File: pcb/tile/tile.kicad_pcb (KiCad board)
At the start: 2 copper layers, 41.5 x 28 mm, 21 parts, among them IC1 THVD1420DR, J1 LED Strip, J2 UPDI, J3 5555140-2, J4 5555140-2, J5 12V, U1 ATtiny3224-X

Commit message: Small tweaks
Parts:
- added R3: 120 Ohm, Resistor_SMD:R_0805_2012Metric_Pad1.20x1.40mm_HandSolder, B.Cu at (161.5, 74.6)
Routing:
- net /SENSE_IN: track 26.1 -> 34.9 mm, vias 3 -> 5
- net /TRCV-A: track 20.7 -> 17.6 mm, vias 0 -> 1
- net /TRCV-B: track 13.1 -> 14.0 mm, vias 0 -> 1

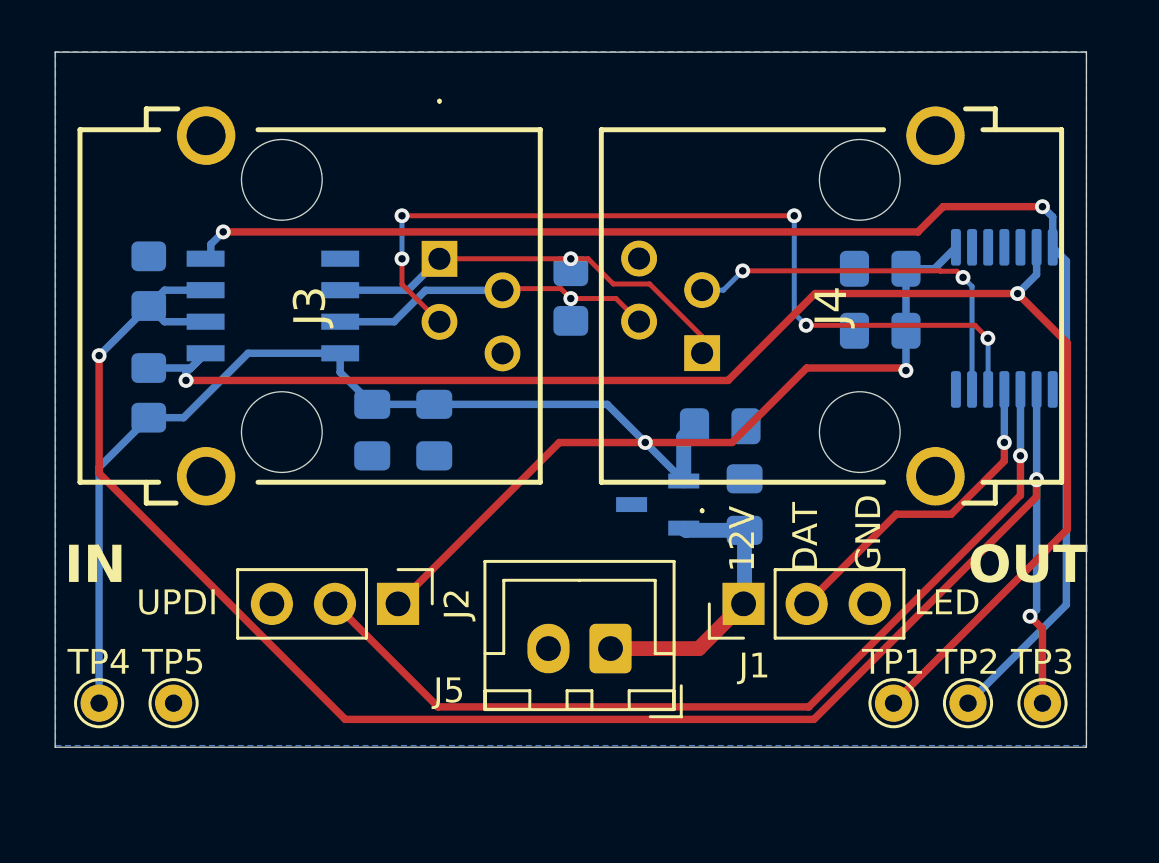
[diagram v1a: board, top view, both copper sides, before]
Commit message: Updated version of the tile that only uses on RJ45 jack vs two RJ12 jacks
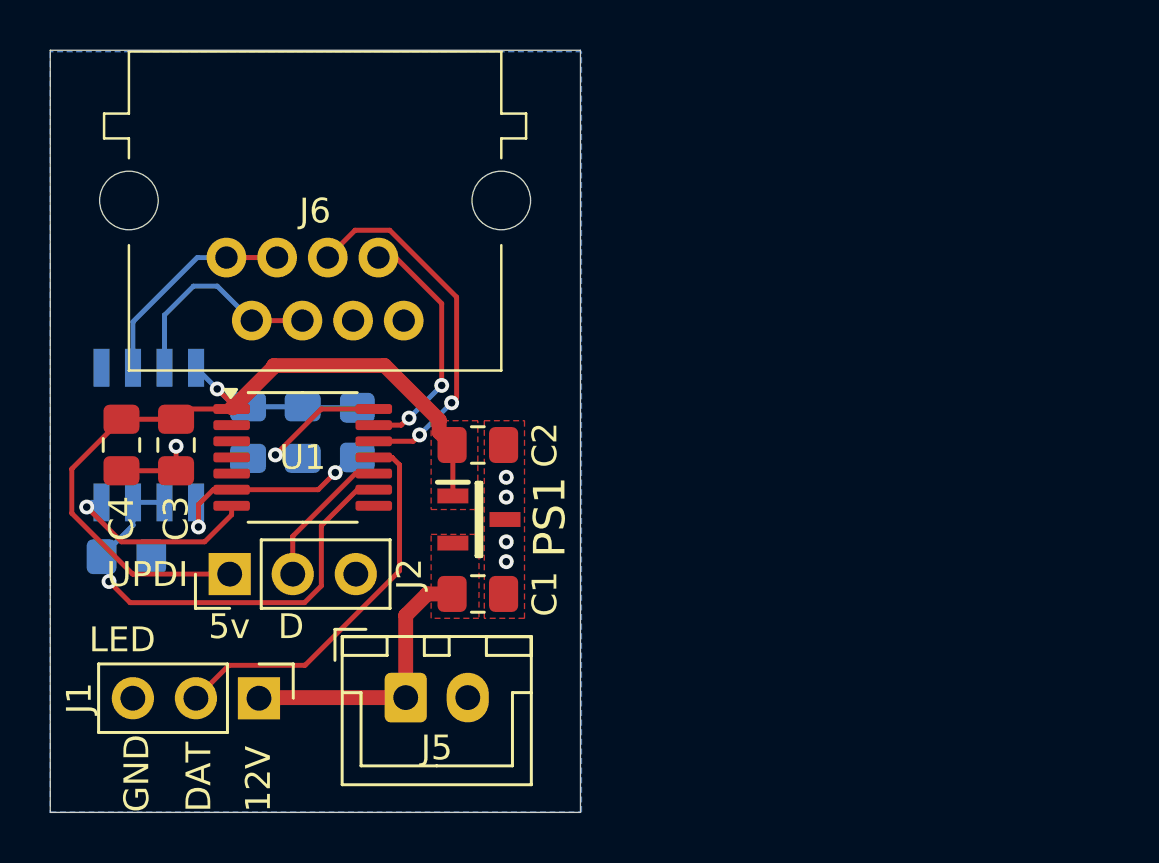
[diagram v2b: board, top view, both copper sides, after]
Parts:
- removed J3, J4: 5555140-2, 5555140-2:55551402
- removed R3: 120 Ohm, Resistor_SMD:R_0805_2012Metric_Pad1.20x1.40mm_HandSolder
- removed TP1: RX, TestPoint:TestPoint_THTPad_D1.5mm_Drill0.7mm
- removed TP2: DX, TestPoint:TestPoint_THTPad_D1.5mm_Drill0.7mm
- removed TP3: XDIR, TestPoint:TestPoint_THTPad_D1.5mm_Drill0.7mm
- removed TP4: 5V, TestPoint:TestPoint_THTPad_D1.5mm_Drill0.7mm
- removed TP5: GND, TestPoint:TestPoint_THTPad_D1.5mm_Drill0.7mm
- added J6: RS-485 Jack, Garth:6P6C RA RJ45 Jack, F.Cu at (151.2, 73.0)
- C1, C2, C3, C4, PS1, U1: moved to F.Cu
- moved C4 30.9 mm to (143.4, 80.6), turned to -90 degrees
- moved C3 29.2 mm to (145.6, 80.6), turned to -90 degrees
- moved U1 28.8 mm to (150.7, 81.1), turned to 0 degrees
- moved J1 19.9 mm to (148.9, 90.8), turned to -90 degrees
- moved C1 11.3 mm to (157.8, 86.6), turned to 0 degrees
- moved R1 11.1 mm to (143.6, 85.1), turned to 0 degrees
- moved C2 9.79 mm to (157.8, 80.6)
- moved R2 8.55 mm to (152.9, 80.1), turned to -90 degrees
- moved J5 8.48 mm to (154.8, 90.8), turned to 0 degrees
- moved PS1 7.22 mm to (157.8, 83.6), turned to 0 degrees
- moved IC1 7.21 mm to (144.5, 80.2), turned to 90 degrees
- moved J2 6.89 mm to (147.8, 85.8), turned to 90 degrees
- moved C6 5.30 mm to (150.7, 80.1)
- moved C5 5.00 mm to (148.5, 80.1)
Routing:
- net /XDIR: track 71.9 -> 19.4 mm, vias 3 -> 1
- net /RxD: track 61.3 -> 9.26 mm
- net /TxD: track 56.8 -> 7.90 mm, vias 2 -> 1
- net +5V: track 70.8 -> 38.0 mm, vias 2 -> 1
- net /UDPI_Data: track 37.1 -> 5.83 mm, vias 1 -> 0
- net /SENSE_IN: track 34.9 -> 14.9 mm, vias 5 -> 2
- net /TRCV-A: track 17.6 -> 8.73 mm, vias 1 -> 0
- net GND: track 0.00 -> 7.92 mm, vias 0 -> 6
- net /SENSE_OUT: track 15.9 -> 10.0 mm
- net /TRCV-B: track 14.0 -> 8.74 mm, vias 1 -> 0
- net /LED_Data: track 13.2 -> 15.8 mm, vias 1 -> 0
- added copper zone on F.Cu, net +12V
- added copper zone on F.Cu, net +5V
- added copper zone on F.Cu, net GND
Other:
- board size 41.5 x 28 mm -> 21.4 x 30.7 mm
- board text added: "5v"
- board text added: "D"
- board text added: "Sin"
- board text added: "Sout"
- board text added: "[BOARD_COST] 0.843in x 1.211in | 1.020 in^2 | $5.10"
- board text added: "v1.1a 2025-10-18"
- board text removed: "IN"
- board text removed: "OUT"
- board text removed: "S"
- board text removed: "v1.1 2025-10-18"
